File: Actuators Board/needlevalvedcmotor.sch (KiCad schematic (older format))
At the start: 51 parts, among them J10 Conn_01x02_Male, J9 Conn_01x02_Male, Q1 MMDT2222A

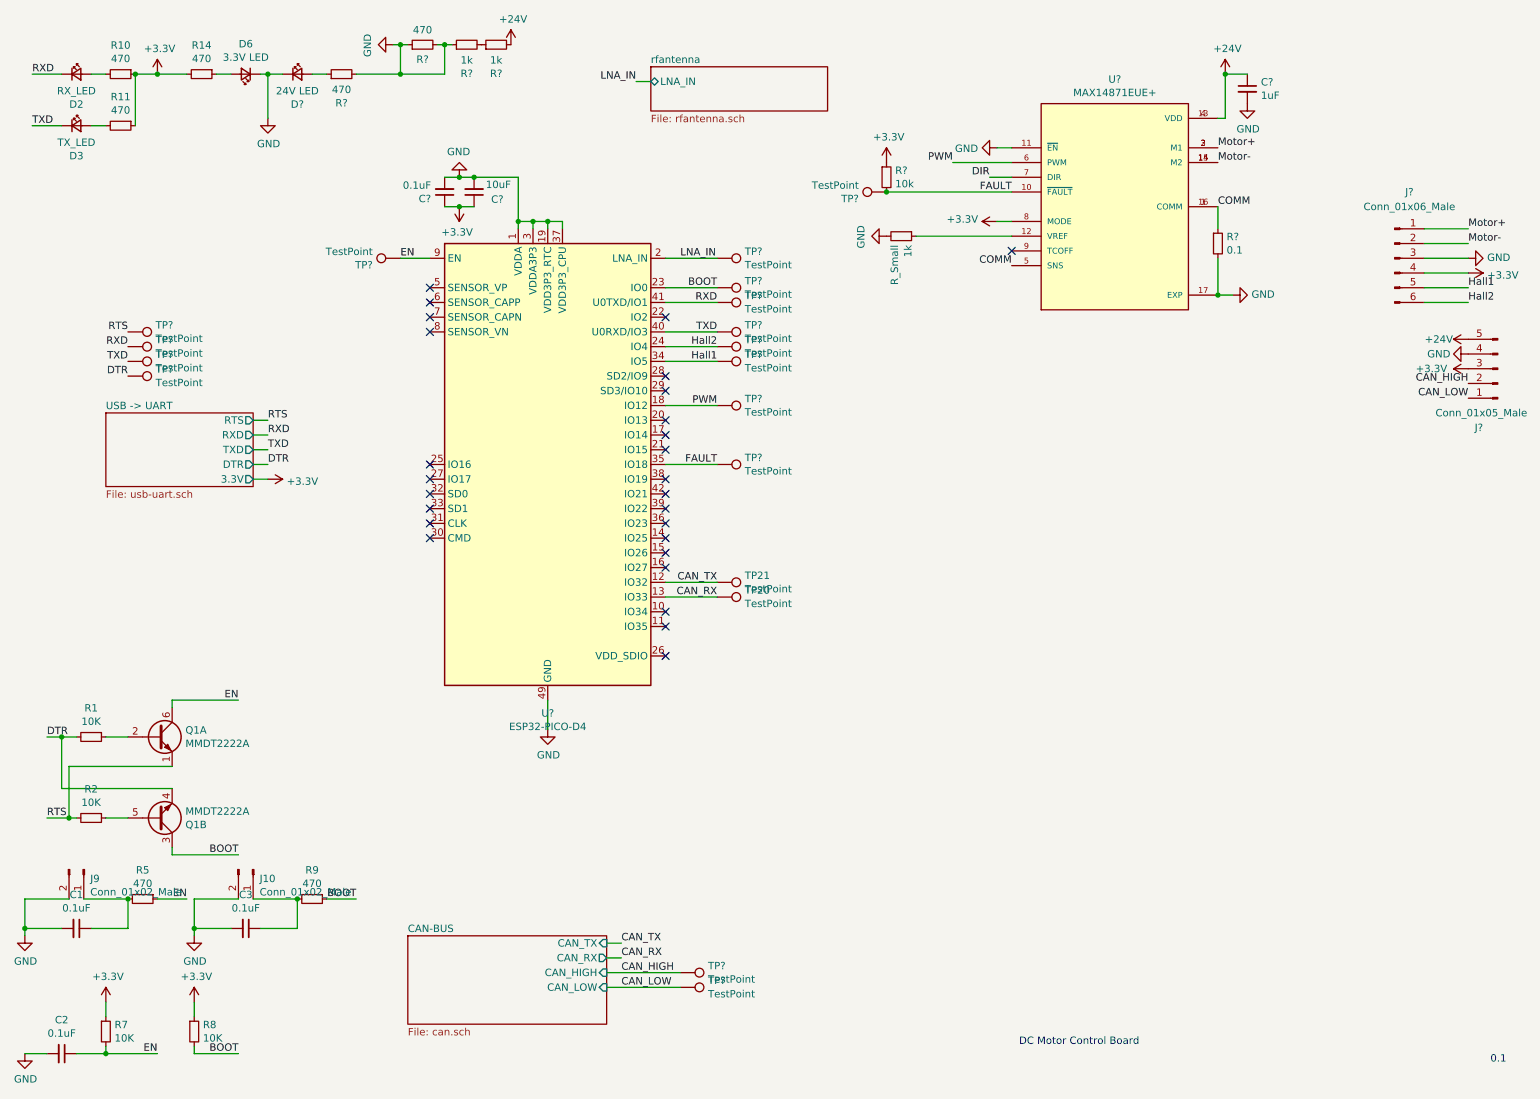
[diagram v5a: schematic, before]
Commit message: Most footprint assignments on dc motor board
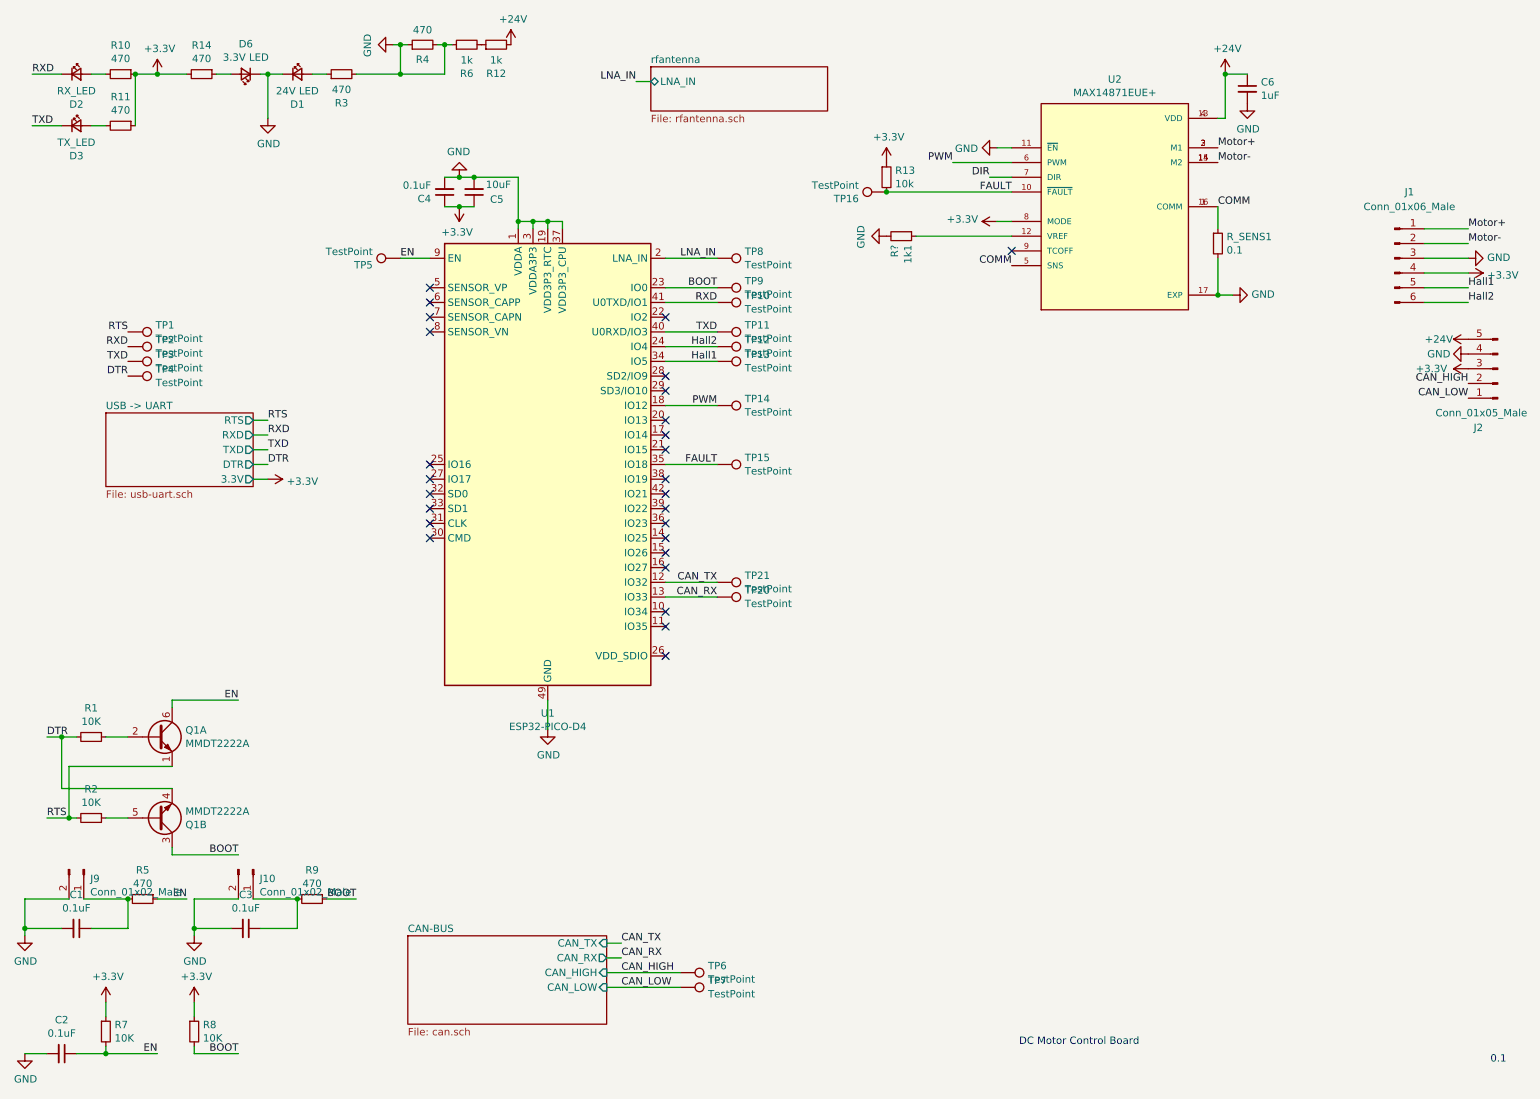
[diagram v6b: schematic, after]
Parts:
- 1k1: renamed from 1k; value R_Small -> R?; footprint (none) -> Resistor_SMD:R_0603_1608Metric
- C4, C5, C6: renamed from C?; footprint (none) -> Capacitor_SMD:C_0603_1608Metric
- J1: renamed from J?; footprint (none) -> Connector_PinHeader_2.54mm:PinHeader_1x05_P2.54mm_Vertical_SMD_Pin1Left
- R13, R_SENS1: renamed from R?; footprint (none) -> Resistor_SMD:R_0603_1608Metric
- TP10, TP11, TP12, TP13, TP14, TP15, TP16, TP5, TP8, TP9: renamed from TP?; footprint (none) -> TestPoint:TestPoint_THTPad_1.0x1.0mm_Drill0.5mm
- U2: renamed from U?; footprint SOP65P637X110-16N -> iclr:SOP65P637X110-16N
- gave numbers to parts that had none: 13

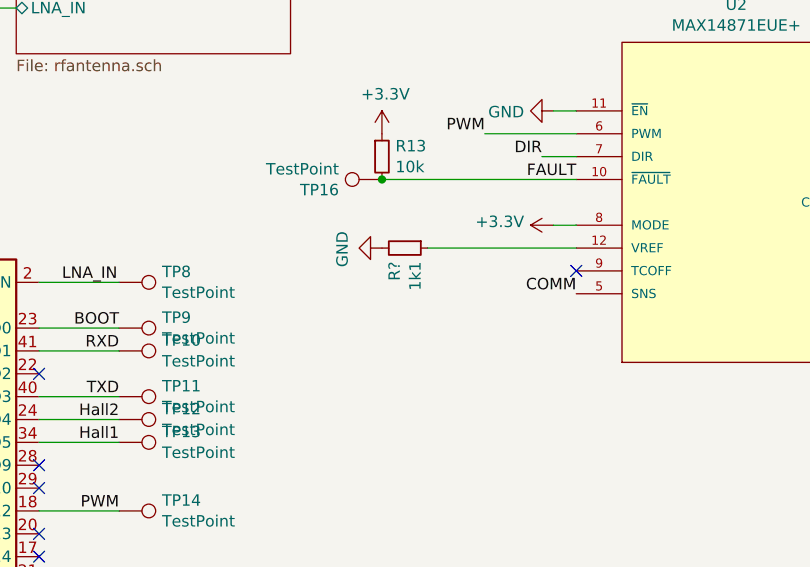
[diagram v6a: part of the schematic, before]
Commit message: More footprint assignments, imported components into PCB
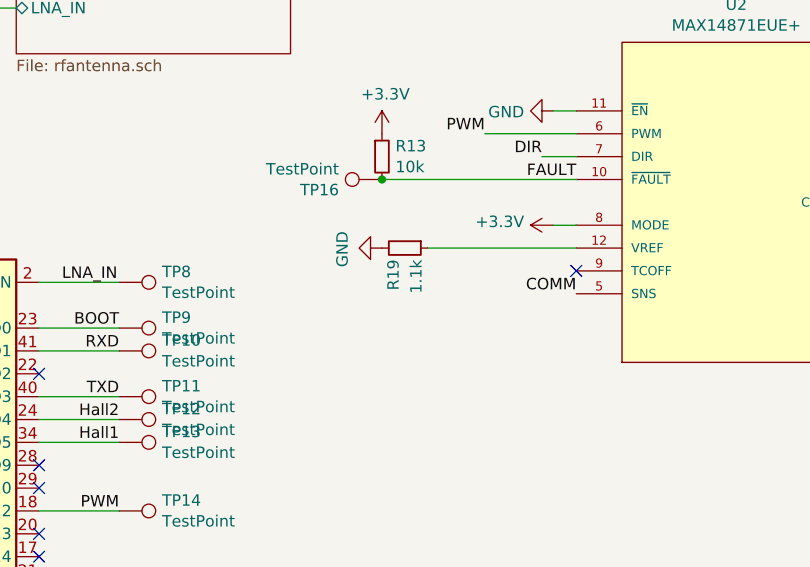
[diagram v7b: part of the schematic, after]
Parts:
- removed 1k1: R?, Resistor_SMD:R_0603_1608Metric, symbol Device:R_Small
- added R19: 1.1k, Resistor_SMD:R_0603_1608Metric, symbol Device:R_Small
- J1: footprint Connector_PinHeader_2.54mm:PinHeader_1x05_P2.54mm_Vertical_SMD_Pin1Left -> Connector_PinSocket_2.54mm:PinSocket_1x06_P2.54mm_Vertical
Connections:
- net GND: now also R19.2
- net at U2.12 (VREF): now also R19.1
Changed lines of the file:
@@
 F 0 "J1" H 10050 2600 50  0000 C CNN
 F 1 "Conn_01x06_Male" H 10050 2500 50  0000 C CNN
-F 2 "Connector_PinHeader_2.54mm:PinHeader_1x05_P2.54mm_Vertical_SMD_Pin1Left" H 9950 2150 50  0001 C CNN
+F 2 "Connector_PinSocket_2.54mm:PinSocket_1x06_P2.54mm_Vertical" H 9950 2150 50  0001 C CNN
 F 3 "~" H 9950 2150 50  0001 C CNN
 	1    9950 2150
@@
 Text Label 7200 1600 2    50   ~ 0
 DIR
-$Comp
-L Device:R_Small 1k1
-U 1 1 6195484F
-P 6600 2000
-F 0 "1k1" H 6659 2046 50  0000 L CNN
-F 1 "R?" H 6659 1955 50  0000 L CNN
-F 2 "Resistor_SMD:R_0603_1608Metric" H 6600 2000 50  0001 C CNN
-F 3 "~" H 6600 2000 50  0001 C CNN
-	1    6600 2000
-	0    1    1    0
-$EndComp
 $Comp
 L power:GND #PWR0102
@@
 Wire Wire Line
 	6500 1700 7350 1700
+$Comp
+L Device:R_Small R19
+U 1 1 61BA7710
+P 6600 2000
+F 0 "R19" H 6650 1950 50  0000 L CNN
+F 1 "1.1k" H 6650 2050 50  0000 L CNN
+F 2 "Resistor_SMD:R_0603_1608Metric" H 6600 2000 50  0001 C CNN
+F 3 "~" H 6600 2000 50  0001 C CNN
+	1    6600 2000
+	0    1    1    0
+$EndComp
 $EndSCHEMATC

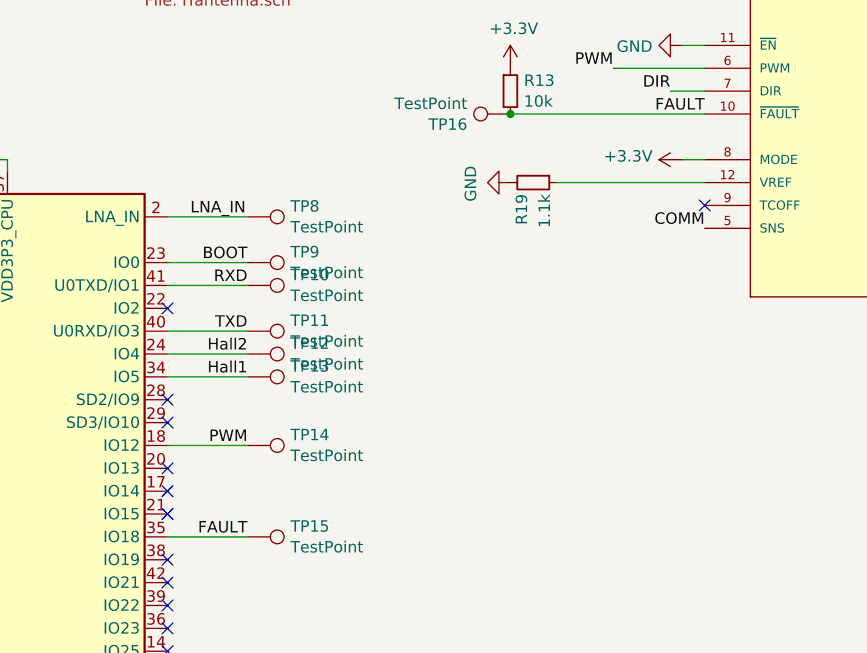
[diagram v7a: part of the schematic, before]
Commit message: Connected H bridge direction select pin to esp32(I forgor)
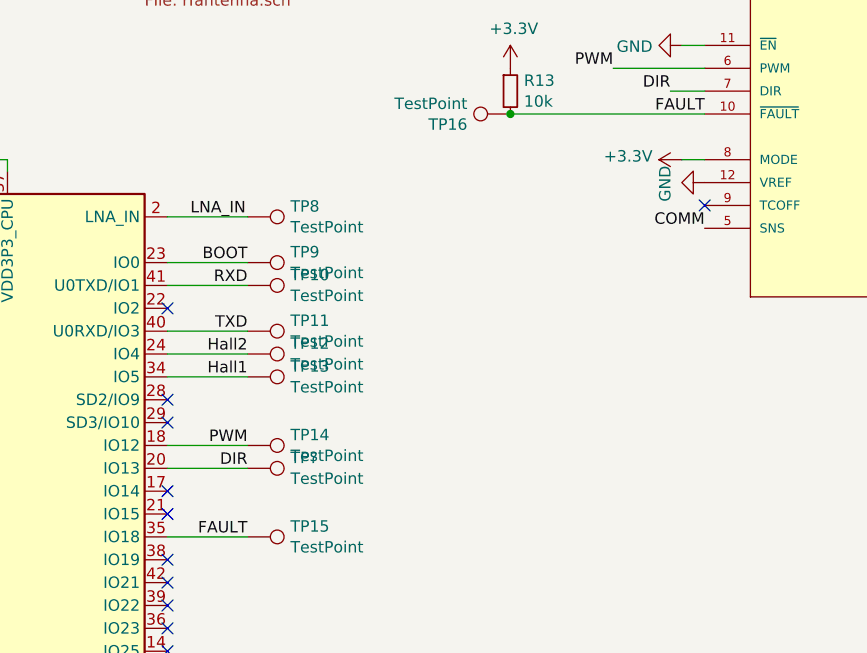
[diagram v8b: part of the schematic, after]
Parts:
- removed R19: 1.1k, Resistor_SMD:R_0603_1608Metric, symbol Device:R_Small
- added TP?: TestPoint, TestPoint:TestPoint_THTPad_1.0x1.0mm_Drill0.5mm, symbol Connector:TestPoint
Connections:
- net DIR: now also U1.20 (IO13), TP?.1
- net GND: now also U2.12 (VREF)
- no-connect marks 27 -> 26
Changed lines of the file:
@@
 DIR
-$Comp
-L power:GND #PWR0102
-U 1 1 6195519D
-P 6500 2000
-F 0 "#PWR0102" H 6500 1750 50  0001 C CNN
-F 1 "GND" H 6505 1827 50  0000 C CNN
-F 2 "" H 6500 2000 50  0001 C CNN
-F 3 "" H 6500 2000 50  0001 C CNN
-	1    6500 2000
-	0    1    1    0
-$EndComp
 $Comp
 L power:+24V #PWR0103
@@
 Wire Wire Line
 	7250 1900 7350 1900
-Wire Wire Line
-	6700 2000 7350 2000
 Wire Wire Line
 	10150 1950 10450 1950
@@
 FAULT
 NoConn ~ 5000 3950
-NoConn ~ 5000 3650
-NoConn ~ 5000 3250
 Text Label 5350 3550 2    50   ~ 0
 FAULT
@@
 	6500 1700 7350 1700
 $Comp
-L Device:R_Small R19
-U 1 1 61BA7710
-P 6600 2000
-F 0 "R19" H 6650 1950 50  0000 L CNN
-F 1 "1.1k" H 6650 2050 50  0000 L CNN
-F 2 "Resistor_SMD:R_0603_1608Metric" H 6600 2000 50  0001 C CNN
-F 3 "~" H 6600 2000 50  0001 C CNN
-	1    6600 2000
-	0    1    1    0
-$EndComp
+L power:GND #PWR0102
+U 1 1 6195519D
+P 7350 2000
+F 0 "#PWR0102" H 7350 1750 50  0001 C CNN
+F 1 "GND" H 7355 1827 50  0000 C CNN
+F 2 "" H 7350 2000 50  0001 C CNN
+F 3 "" H 7350 2000 50  0001 C CNN
+	1    7350 2000
+	0    1    1    0
+$EndComp
+NoConn ~ 5000 3650
+Wire Wire Line
+	5000 3250 5350 3250
+$Comp
+L Connector:TestPoint TP?
+U 1 1 61CE7E78
+P 5350 3250
+F 0 "TP?" V 5304 3438 50  0000 L CNN
+F 1 "TestPoint" V 5395 3438 50  0000 L CNN
+F 2 "TestPoint:TestPoint_THTPad_1.0x1.0mm_Drill0.5mm" H 5550 3250 50  0001 C CNN
+F 3 "~" H 5550 3250 50  0001 C CNN
+	1    5350 3250
+	0    1    1    0
+$EndComp
+Text Label 5350 3250 2    50   ~ 0
+DIR
 $EndSCHEMATC
